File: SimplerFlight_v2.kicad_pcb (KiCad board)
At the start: 2 copper layers, 93.8 x 73.5 mm, 116 parts, among them J1 Battery 1, J10 Cam 3, J11 Servo, J12 Cam 2, J13 SWD Header, J14 DM3CS-SF, J2 Encoder, J7 Battery 2, J8 USB, J9 Cam 1, Q1 BSS816NWH6327XTSA1, Q2 NPN, Q3 BSS816NWH6327XTSA1, Q6 BSS816NWH6327XTSA1, SW1 Boot Switch, SW2 System Reset, U1 AMS1117-3.3, U2 STM32F401RETx, U3 BMP581, U4 BNO085, U5 TPS56A37RPAR, U6 TPS56A37RPAR, U7 MX25V4006EM1I-13G, Y2 Crystal

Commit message: symc
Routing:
- net /Microcontroller/SD_DET: track 3.82 -> 37.2 mm
- net /Headers/+3V3: track 248.1 -> 250.1 mm
- net GND: track 107.8 -> 109.3 mm, vias 55 -> 56
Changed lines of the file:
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@@
 	)
 	(segment
+		(start 231.074 107.249)
+		(end 231.013 107.188)
+		(width 0.3)
+		(layer "F.Cu")
+		(net 1)
+	)
+	(segment
 		(start 199.833513 111.570487)
 		(end 199.517 111.887)
@@
 	)
 	(segment
+		(start 232.41 107.249)
+		(end 231.074 107.249)
+		(width 0.3)
+		(layer "F.Cu")
+		(net 1)
+	)
+	(segment
 		(start 194.9 92.8388)
 		(end 196.8888 92.8388)
@@
 	)
 	(via
+		(at 231.013 107.188)
+		(size 0.6)
+		(drill 0.3)
+		(layers "F.Cu" "B.Cu")
+		(net 1)
+	)
+	(via
 		(at 204.343 110.49)
 		(size 0.7)
@@
 	)
 	(segment
+		(start 213.233 132.436364)
+		(end 211.860636 131.064)
+		(width 0.3)
+		(layer "F.Cu")
+		(net 30)
+	)
+	(segment
+		(start 219.7 143.35)
+		(end 217.447 141.097)
+		(width 0.3)
+		(layer "F.Cu")
+		(net 30)
+	)
+	(segment
+		(start 217.447 141.097)
+		(end 213.233 141.097)
+		(width 0.3)
+		(layer "F.Cu")
+		(net 30)
+	)
+	(segment
 		(start 223.55 107.475)
 		(end 223.55 108.936)
@@
 	)
 	(segment
+		(start 206.883 131.064)
+		(end 206.883 120.634)
+		(width 0.3)
+		(layer "F.Cu")
+		(net 30)
+	)
+	(segment
+		(start 211.860636 131.064)
+		(end 206.883 131.064)
+		(width 0.3)
+		(layer "F.Cu")
+		(net 30)
+	)
+	(segment
 		(start 223.55 108.936)
 		(end 222.377 110.109)
@@
 	)
 	(segment
+		(start 213.233 141.097)
+		(end 213.233 132.436364)
+		(width 0.3)
+		(layer "F.Cu")
+		(net 30)
+	)
+	(segment
 		(start 236.379965 104.549)
 		(end 236.379965 103.918965)
@@
 		(width 0.5)
 		(layer "F.Cu")
+		(net 76)
+	)
+	(segment
+		(start 206.883 118.634)
+		(end 208.915 118.634)
+		(width 0.5)
+		(layer "F.Cu")

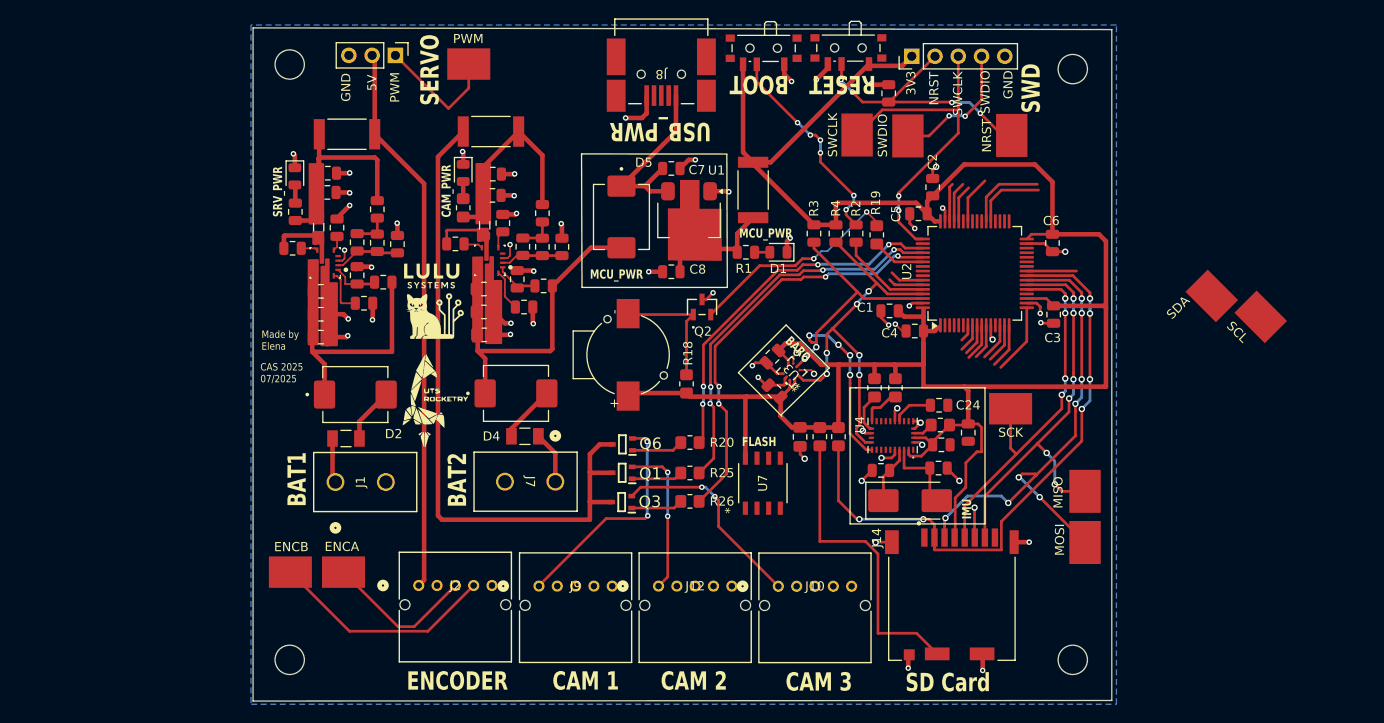
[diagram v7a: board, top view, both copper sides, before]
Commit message: Finish all essential routing
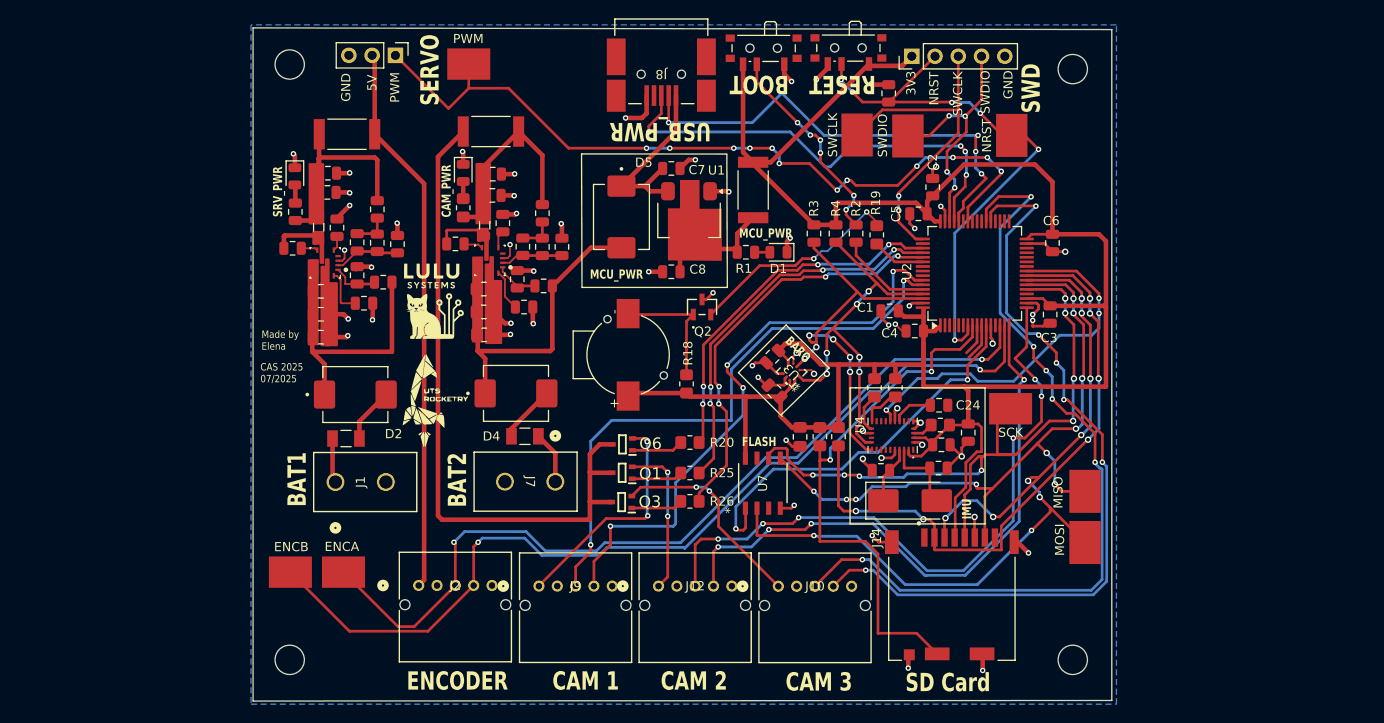
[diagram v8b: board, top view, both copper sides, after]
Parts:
- removed SCL, SDA: 5016, 5016:KEYSTONE_5016
- moved C3 0.38 mm to (232.0, 106.3)
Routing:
- net /Microcontroller/USART6_RX: track 8.82 -> 89.6 mm, vias 0 -> 6
- net /Microcontroller/USART6_TX: track 7.95 -> 86.3 mm, vias 0 -> 6
- net /Microcontroller/ENC_A: track 20.7 -> 93.9 mm, vias 0 -> 2
- net /Microcontroller/ENC_B: track 29.1 -> 101.4 mm, vias 0 -> 2
- net /Microcontroller/SERVO_PWM: track 19.2 -> 86.8 mm, vias 0 -> 12
- net /Microcontroller/USART2_RX: track 7.71 -> 72.2 mm, vias 0 -> 6
- net /Microcontroller/USART1_RX: track 3.85 -> 64.6 mm, vias 0 -> 2
- net /Microcontroller/USART2_TX: track 4.95 -> 65.5 mm, vias 0 -> 4
- net /Microcontroller/USART1_TX: track 3.71 -> 63.6 mm, vias 0 -> 4
- net /Microcontroller/USB_OTG_FS_D-: track 4.12 -> 51.1 mm, vias 0 -> 4
- net /Microcontroller/USB_OTG_FS_D+: track 4.45 -> 50.1 mm, vias 0 -> 4
- net /Microcontroller/SPI1_MOSI: track 55.5 -> 96.8 mm, vias 8 -> 10
- net /Microcontroller/FLASH_MEM_CS: track 3.89 -> 43.6 mm, vias 0 -> 2
- net /Microcontroller/IMU_RST: track 5.43 -> 41.7 mm, vias 0 -> 3
- net /Microcontroller/SPI1_SCK: track 40.8 -> 75.5 mm, vias 4 -> 8
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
